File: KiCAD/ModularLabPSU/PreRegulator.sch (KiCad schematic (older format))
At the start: 27 parts, among them Q5 IRFP5210, Q6 IRFP5210, Q7 BC847B, U12 SCR, U13 LT1716, U7 LT1639

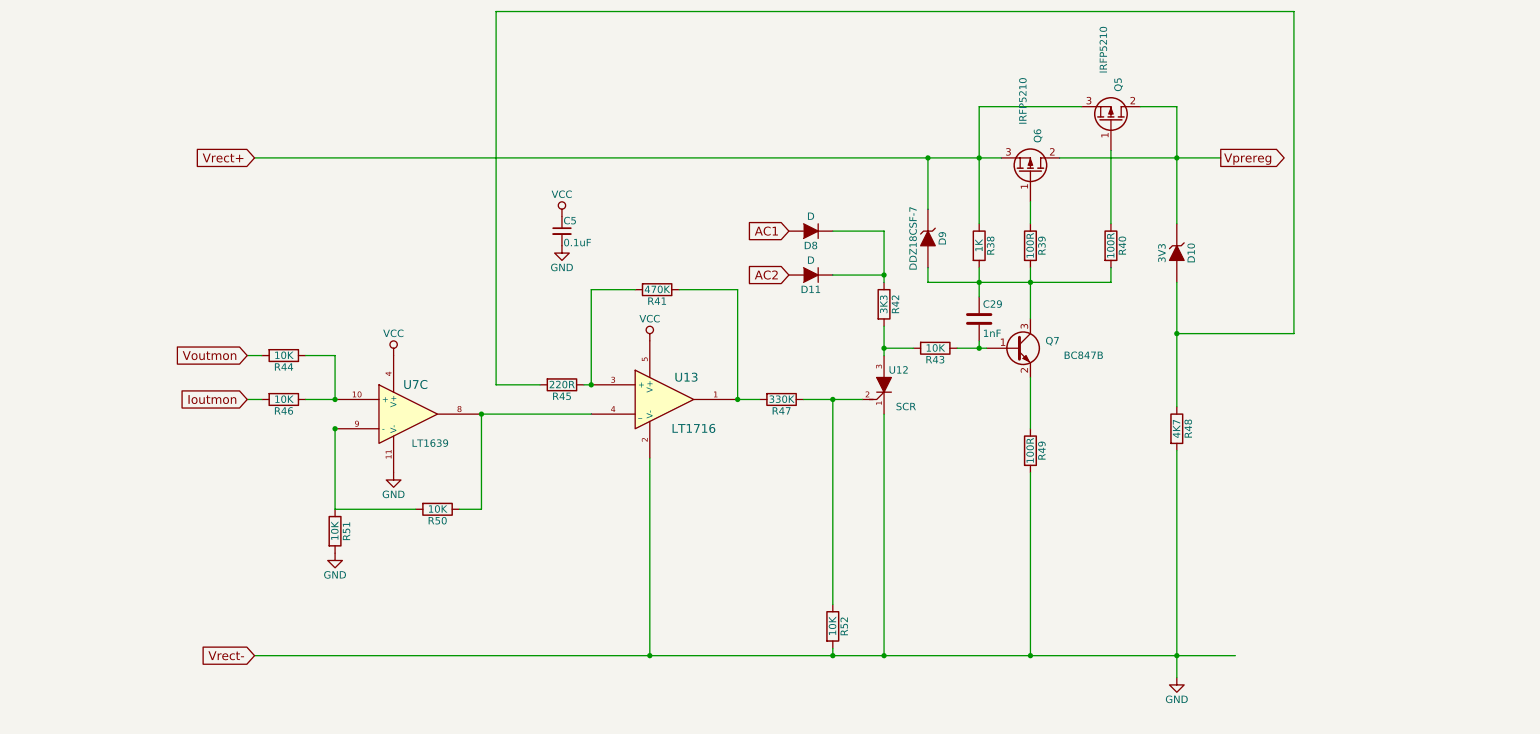
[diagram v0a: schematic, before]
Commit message: Started re-design of PCB. Schematic changes from testing first board and started developing new layout
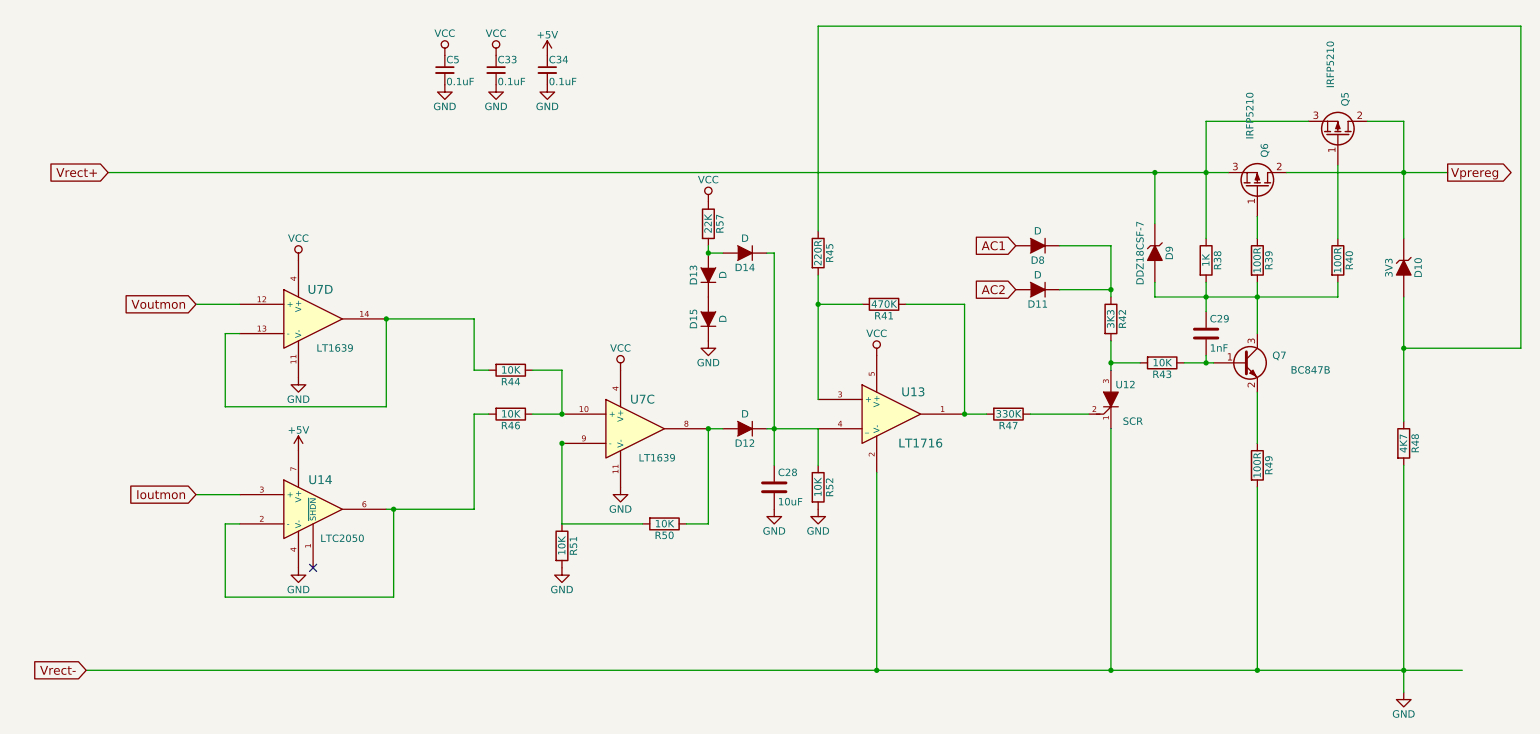
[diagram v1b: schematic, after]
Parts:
- added C28: 10uF, Capacitors_SMD:C_0805_HandSoldering, symbol C
- added C33, C34: 0.1uF, Capacitors_SMD:C_0805_HandSoldering, symbol C_Small
- added D12, D13, D14, D15: D, Diodes_SMD:SOD-323, symbol D
- added R57: 22K, Resistors_SMD:R_0805_HandSoldering, symbol R
- added U14: LTC2050, Housings_SOIC:SOIC-8_3.9x4.9mm_Pitch1.27mm, symbol LTC2050
- added unit 4 of U7
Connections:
- net GND: now also C28.2, C33.2, C34.2, D15.1 (K), U14.4 (V-), U7.11 (V-)
- net Ioutmon: now also U14.3 (+); no longer R46.2
- net VCC: now also C33.1, R57.1, U7.4 (V+)
- net Voutmon: now also U7.12 (+); no longer R44.2
- net at R47.1, U12.2: no longer R52.1
- net at R41.2, U13.3 (+): now also R45.2; no longer R45.1
- net at D10.2 (A), R48.1: now also R45.1; no longer R45.2
- net at R50.1, U7.8: now also D12.2 (A); no longer U13.4 (_)
- new net: R44.2, U7.13 (-), U7.14
- new net: R46.2, U14.2 (-), U14.6
- new net: C28.1, D12.1 (K), D14.1 (K), R52.1, U13.4 (_)
- new net: D13.1 (K), D15.2 (A)
- new net: D13.2 (A), D14.2 (A), R57.2
- new net +5V: C34.1, U14.7 (V+)
- no-connect marks 0 -> 1
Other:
- moved on the sheet: C29, C5, D10, D11, D8, D9, Q5, Q6, Q7, R38, R39, R40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
